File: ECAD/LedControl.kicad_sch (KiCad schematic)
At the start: 4 parts, among them Q3 NCE3018AS, Q4 NCE3018AS, Q5 NCE3018AS, Q6 NCE3018AS

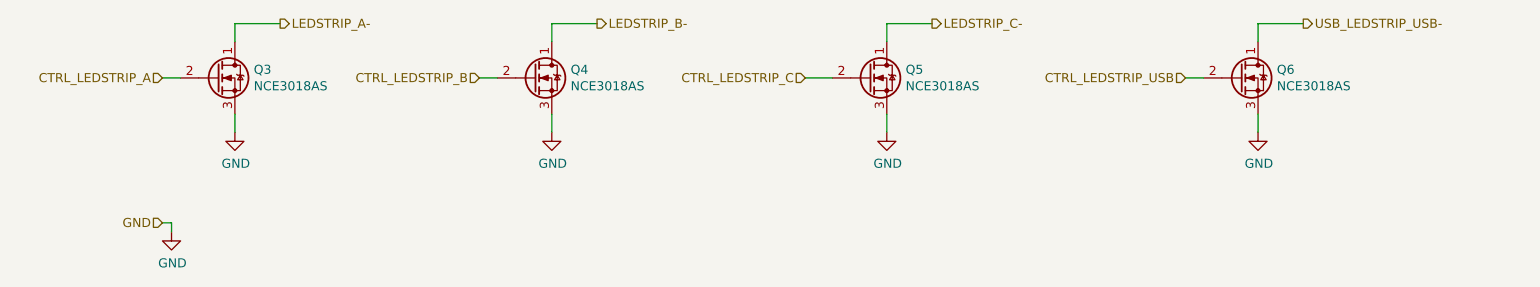
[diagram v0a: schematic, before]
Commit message: finishing up pcb, only billonly bill of materials need to be done to be compatible with lc from jlcpcb
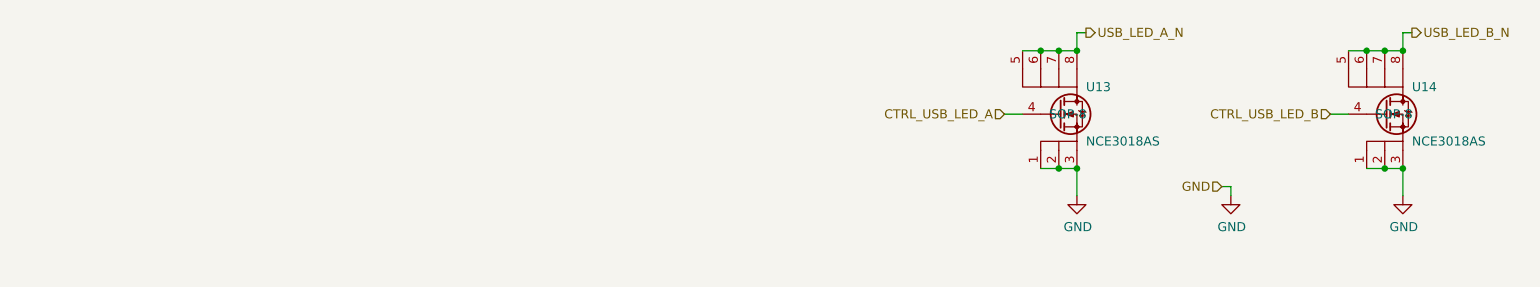
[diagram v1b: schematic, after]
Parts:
- removed Q3, Q4, Q5, Q6: NCE3018AS, Package_SO:SOP-8_3.9x4.9mm_P1.27mm, symbol Device:Q_NMOS_DGS
- added U13, U14: NCE3018AS, Package_SO:SO-8_3.9x4.9mm_P1.27mm, symbol Transistors:NCE3018AS
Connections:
- net GND: now also U13.1, U13.2, U13.3, U14.1, U14.2, U14.3
- new net CTRL_USB_LED_A: U13.4
- new net CTRL_USB_LED_B: U14.4
- new net USB_LED_A_N: U13.5, U13.6, U13.7, U13.8
- new net USB_LED_B_N: U14.5, U14.6, U14.7, U14.8

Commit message: adding production and step files
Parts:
- U13, U14: Package SOP-8 -> SOP-8_150mil
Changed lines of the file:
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@@
       (effects (font (size 1.27 1.27)) hide)
     )
-    (property "Package" "SOP-8" (id 5) (at 170.18 97.79 0))
+    (property "Package" "SOP-8_150mil" (id 5) (at 170.18 97.79 0))
     (property "Manufacturer" "NCE Power" (id 6) (at 179.07 99.06 0)
       (effects (font (size 1.27 1.27)) hide)
@@
       (effects (font (size 1.27 1.27)) hide)
     )
-    (property "Package" "SOP-8" (id 5) (at 215.9 97.79 0))
+    (property "Package" "SOP-8_150mil" (id 5) (at 215.9 97.79 0))
     (property "Manufacturer" "NCE Power" (id 6) (at 215.9 97.79 0)
       (effects (font (size 1.27 1.27)) hide)
